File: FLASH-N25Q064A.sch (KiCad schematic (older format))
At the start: 1 part

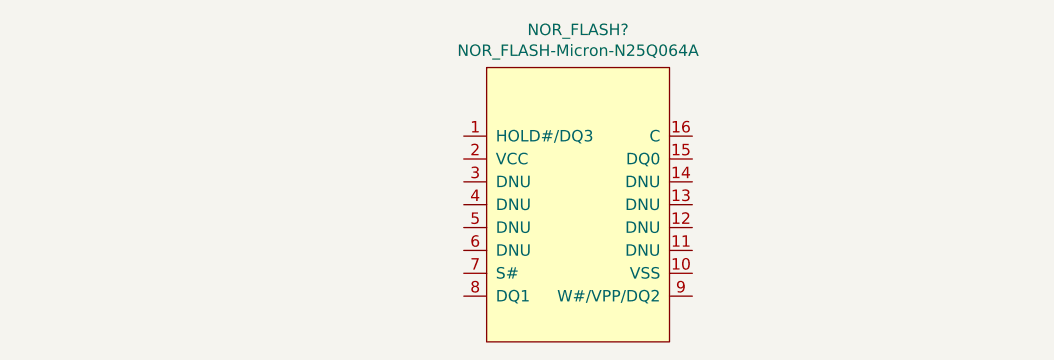
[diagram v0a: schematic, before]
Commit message: LPC + ROM + RAM sch
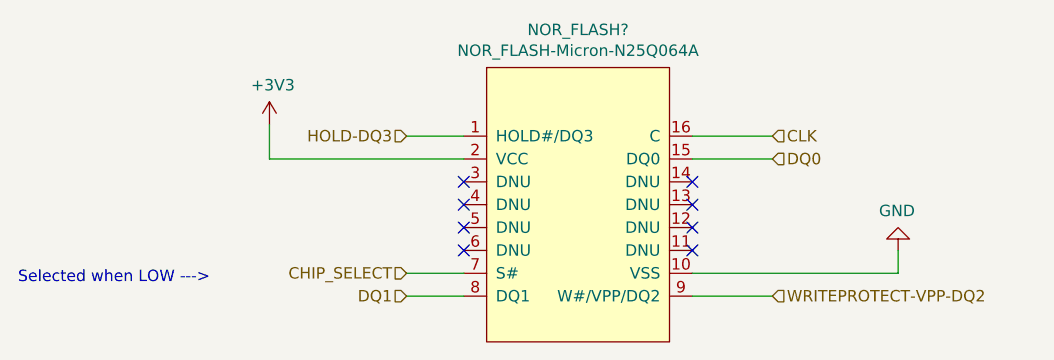
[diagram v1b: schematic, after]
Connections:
- net HOLD-DQ3: now reaches NOR_FLASH?.1 (HOLD#/DQ3)
- net GND: now reaches NOR_FLASH?.10 (VSS)
- net DQ0: now reaches NOR_FLASH?.15 (DQ0)
- net CLK: now reaches NOR_FLASH?.16 (C)
- net +3V3: now reaches NOR_FLASH?.2 (VCC)
- net CHIP_SELECT: now reaches NOR_FLASH?.7 (S#)
- net DQ1: now reaches NOR_FLASH?.8 (DQ1)
- net WRITEPROTECT-VPP-DQ2: now reaches NOR_FLASH?.9 (W#/VPP/DQ2)
- no-connect marks 0 -> 8
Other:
- note added: "Selected when LOW --->"
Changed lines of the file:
@@
 $Descr A4 11693 8268
 encoding utf-8
-Sheet 4 5
+Sheet 6 13
 Title ""
 Date ""
@@
 U 1 1 5F5FA40A
 P 5200 2800
+AR Path="/5F64163B/5F673E59/5F5FA40A" Ref="NOR_FLASH?"  Part="1"
+AR Path="/5F64163B/5F61096F/5F5FA40A" Ref="NOR_FLASH?"  Part="1"
+AR Path="/5F64163B/5F610B6B/5F5FA40A" Ref="NOR_FLASH?"  Part="1"
+AR Path="/5F64163B/5F610D67/5F5FA40A" Ref="NOR_FLASH?"  Part="1"
+AR Path="/5F64163B/5F610FC5/5F5FA40A" Ref="NOR_FLASH?"  Part="1"
+AR Path="/5F64163B/5F61114A/5F5FA40A" Ref="NOR_FLASH?"  Part="1"
+AR Path="/5F64163B/5F611434/5F5FA40A" Ref="NOR_FLASH?"  Part="1"
+AR Path="/5F64163B/5F6116C3/5F5FA40A" Ref="NOR_FLASH?"  Part="1"
 F 0 "NOR_FLASH?" H 5600 2965 50  0000 C CNN
 F 1 "NOR_FLASH-Micron-N25Q064A" H 5600 2874 50  0000 C CNN
@@
 	1    0    0    -1
 $EndComp
+NoConn ~ 5100 3300
+NoConn ~ 5100 3400
+NoConn ~ 5100 3500
+NoConn ~ 5100 3600
+NoConn ~ 6100 3300
+NoConn ~ 6100 3400
+NoConn ~ 6100 3500
+NoConn ~ 6100 3600
+Wire Wire Line
+	4250 3200 4250 3050
+Wire Wire Line
+	4250 3200 5100 3200
+$Comp
+L power:+3V3 #PWR?
+U 1 1 5F5E7279
+P 4250 3050
+AR Path="/5F64163B/5F673E59/5F5E7279" Ref="#PWR?"  Part="1"
+AR Path="/5F64163B/5F61096F/5F5E7279" Ref="#PWR?"  Part="1"
+AR Path="/5F64163B/5F610B6B/5F5E7279" Ref="#PWR?"  Part="1"
+AR Path="/5F64163B/5F610D67/5F5E7279" Ref="#PWR?"  Part="1"
+AR Path="/5F64163B/5F610FC5/5F5E7279" Ref="#PWR?"  Part="1"
+AR Path="/5F64163B/5F61114A/5F5E7279" Ref="#PWR?"  Part="1"
+AR Path="/5F64163B/5F611434/5F5E7279" Ref="#PWR?"  Part="1"
+AR Path="/5F64163B/5F6116C3/5F5E7279" Ref="#PWR?"  Part="1"
+F 0 "#PWR?" H 4250 2900 50  0001 C CNN
+F 1 "+3V3" H 4265 3223 50  0000 C CNN
+F 2 "" H 4250 3050 50  0001 C CNN
+F 3 "" H 4250 3050 50  0001 C CNN
+	1    4250 3050
+	1    0    0    -1
+$EndComp
+Wire Wire Line
+	6100 3700 7000 3700
+Wire Wire Line
+	7000 3700 7000 3600
+$Comp
+L power:GND #PWR?
+U 1 1 5F5E78B9
+P 7000 3600
+AR Path="/5F64163B/5F673E59/5F5E78B9" Ref="#PWR?"  Part="1"
+AR Path="/5F64163B/5F61096F/5F5E78B9" Ref="#PWR?"  Part="1"
+AR Path="/5F64163B/5F610B6B/5F5E78B9" Ref="#PWR?"  Part="1"
+AR Path="/5F64163B/5F610D67/5F5E78B9" Ref="#PWR?"  Part="1"
+AR Path="/5F64163B/5F610FC5/5F5E78B9" Ref="#PWR?"  Part="1"
+AR Path="/5F64163B/5F61114A/5F5E78B9" Ref="#PWR?"  Part="1"
+AR Path="/5F64163B/5F611434/5F5E78B9" Ref="#PWR?"  Part="1"
+AR Path="/5F64163B/5F6116C3/5F5E78B9" Ref="#PWR?"  Part="1"
+F 0 "#PWR?" H 7000 3350 50  0001 C CNN
+F 1 "GND" H 7005 3427 50  0000 C CNN
+F 2 "" H 7000 3600 50  0001 C CNN
+F 3 "" H 7000 3600 50  0001 C CNN
+	1    7000 3600
+	-1   0    0    1
+$EndComp
+Text HLabel 4850 3700 0    50   Input ~ 0
+CHIP_SELECT
+Wire Wire Line
+	5100 3700 4850 3700
+Text Notes 3150 3750 0    50   ~ 0
+Selected when LOW --->
+Text HLabel 6450 3200 2    50   Input ~ 0
+DQ0
+Wire Wire Line
+	6100 3200 6450 3200
+Text HLabel 4850 3800 0    50   Input ~ 0
+DQ1
+Wire Wire Line
+	5100 3800 4850 3800
+Text HLabel 4850 3100 0    50   Input ~ 0
+HOLD-DQ3
+Wire Wire Line
+	5100 3100 4850 3100
+Wire Wire Line
+	6100 3100 6450 3100
+Wire Wire Line
+	6100 3800 6450 3800
+Text HLabel 6450 3800 2    50   Input ~ 0
+WRITEPROTECT-VPP-DQ2
+Text HLabel 6450 3100 2    50   Input ~ 0
+CLK
 $EndSCHEMATC
